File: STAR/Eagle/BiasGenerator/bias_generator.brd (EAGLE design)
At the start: 60.9 x 30.1 mm, 24 parts, among them J1 J30J-9J30, T1 750311838, U1 LT8300, U2 LT8330

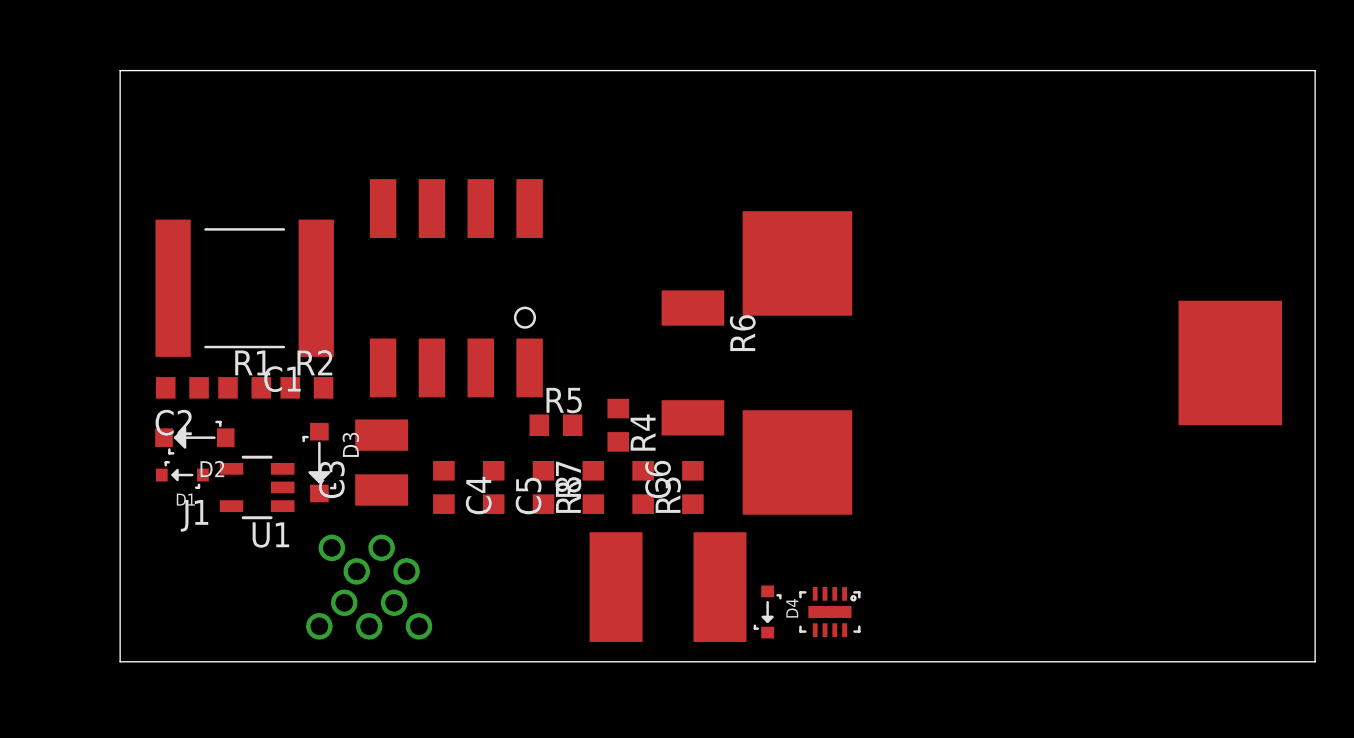
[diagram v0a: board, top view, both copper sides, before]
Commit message: datalogger differential pairs
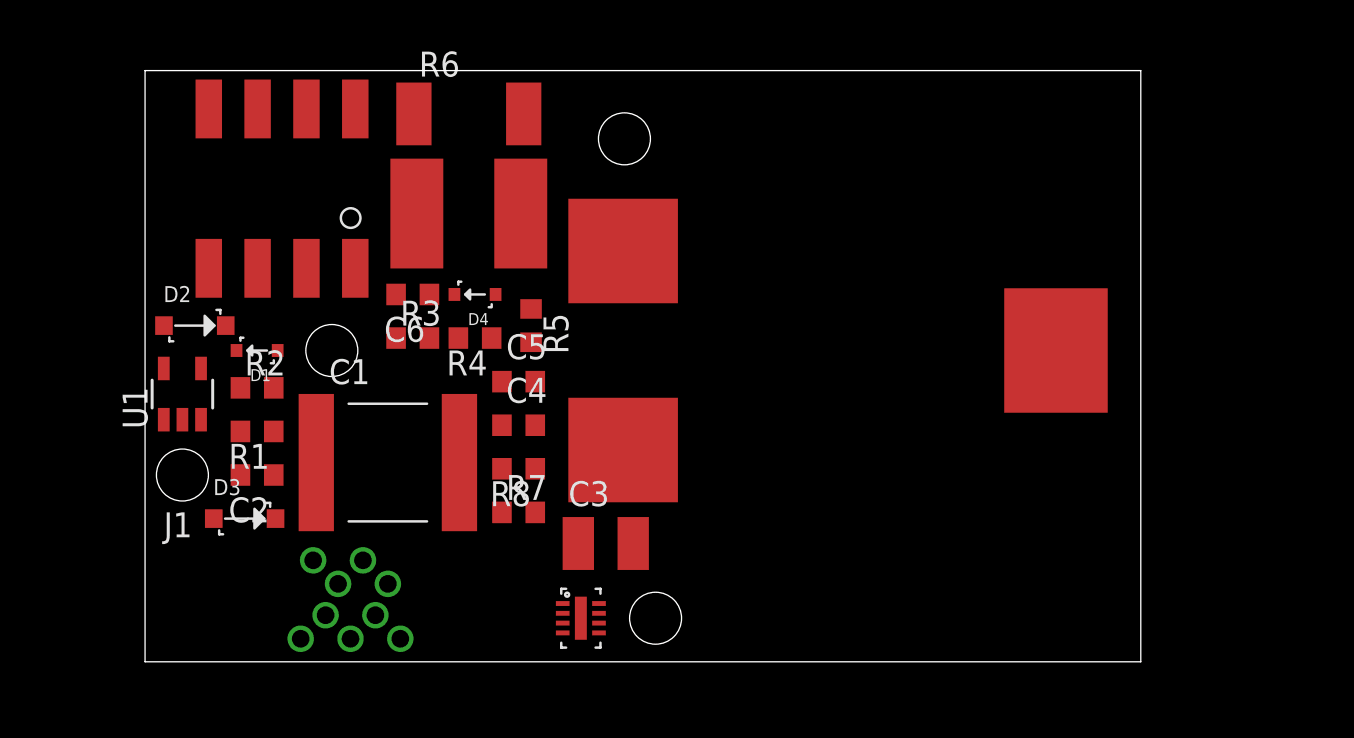
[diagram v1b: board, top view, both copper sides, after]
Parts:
- moved D4 22.0 mm to (16.8, 18.7), turned to 180 degrees
- moved C7 21.6 mm to (16.5, 22.9)
- moved C6 17.3 mm to (13.7, 18.7), turned to 180 degrees
- moved R6 17.1 mm to (16.5, 27.9), turned to 0 degrees
- moved R3 14.0 mm to (13.7, 16.5), turned to 0 degrees
- moved U2 12.7 mm to (22.2, 2.22), turned to 270 degrees
- moved C3 12.2 mm to (23.5, 6.03), turned to 0 degrees
- moved C1 11.5 mm to (12.4, 10.2), turned to 0 degrees
- moved T1 10.2 mm to (6.99, 24.1)
- moved L1 8.91 mm to (38.7, 15.9)
- moved R4 8.55 mm to (16.8, 16.5), turned to 180 degrees
- moved D1 7.41 mm to (5.71, 15.9)
- moved U1 6.10 mm to (1.91, 13.7), turned to 0 degrees
- moved C2 5.85 mm to (5.71, 9.53)
- moved D2 5.71 mm to (2.54, 17.1), turned to 0 degrees
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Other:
- board size 60.9 x 30.1 mm -> 50.8 x 30.1 mm

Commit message: M2 drills
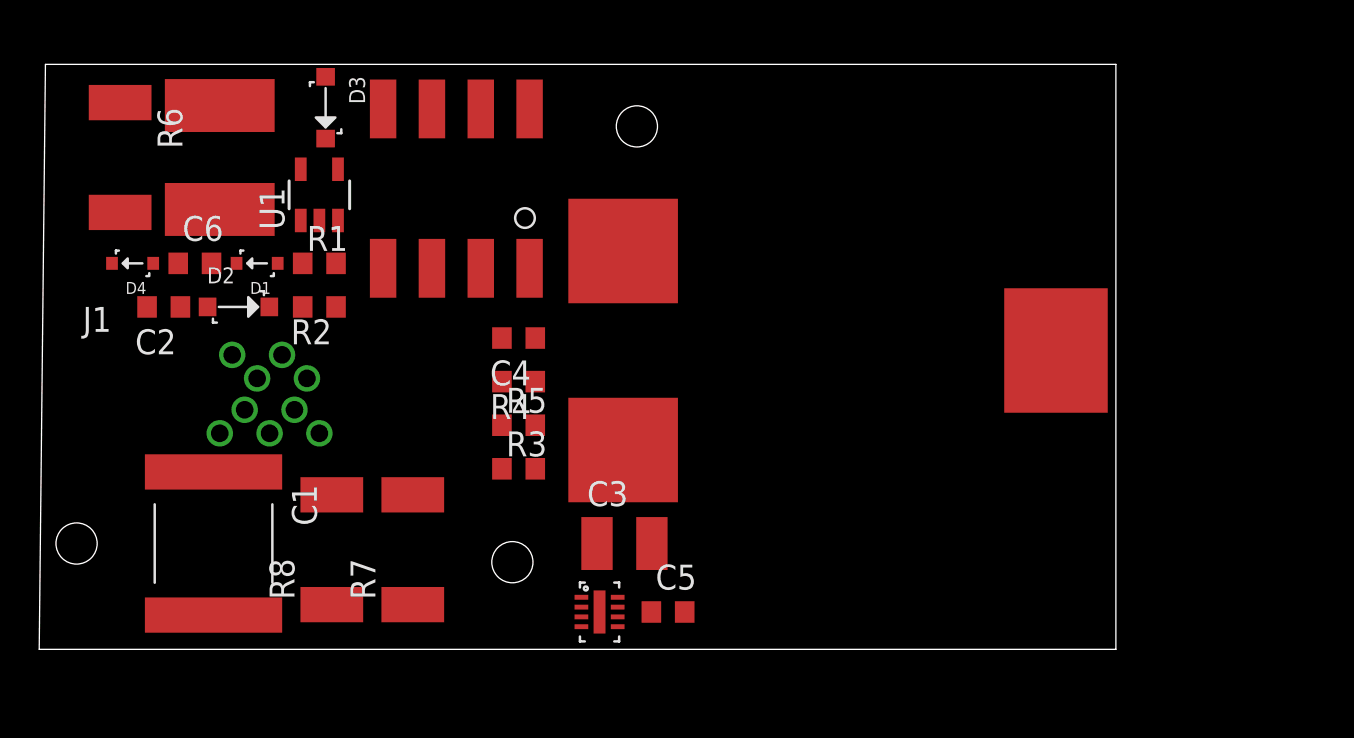
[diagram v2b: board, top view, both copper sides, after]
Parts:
- R7: value 47000 -> 47k; device resistor:R0603 -> resistor:R2512
- R8: value 3000 -> 3k; device resistor:R0603 -> resistor:R2512
- moved D3 21.4 mm to (9.21, 28.3), turned to 270 degrees
- moved R6 17.9 mm to (-1.27, 25.7), turned to 270 degrees
- moved D4 17.5 mm to (-0.64, 20.3)
- moved C5 14.0 mm to (26.7, 2.54)
- moved C7 13.0 mm to (3.81, 25.7), turned to 90 degrees
- moved U1 12.3 mm to (8.89, 23.8)
- moved J1 11.3 mm to (6.35, 13.7)
- moved C6 11.2 mm to (2.54, 20.3), turned to 0 degrees
- moved R8 10.4 mm to (9.53, 5.71), turned to 90 degrees
- moved C2 9.81 mm to (0.95, 18.1)
- moved C1 9.80 mm to (3.49, 6.03), turned to 270 degrees
- moved R1 9.14 mm to (8.89, 20.3), turned to 0 degrees
- moved T1 8.89 mm to (15.9, 24.1)
- moved R3 8.58 mm to (19.1, 9.84)
- moved R7 5.72 mm to (13.7, 5.71), turned to 90 degrees
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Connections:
- removed net N$18: J1.8
- removed net N$19: J1.9
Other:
- board size 50.8 x 30.1 mm -> 54.9 x 29.8 mm

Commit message: bias gen board
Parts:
- moved R7 5.08 mm to (18.7, 5.71)
- moved C1 5.08 mm to (8.57, 6.03)
- moved C2 5.08 mm to (6.03, 18.1)
- moved C6 5.08 mm to (7.62, 20.3)
- moved C7 5.08 mm to (8.89, 25.7)
- moved D1 5.08 mm to (10.8, 20.3)
- moved D4 5.08 mm to (4.45, 20.3)
- moved J1 5.08 mm to (11.4, 13.7)
- moved R1 5.08 mm to (14.0, 20.3)
- moved R2 5.08 mm to (14.0, 18.1)
- moved R6 5.08 mm to (3.81, 25.7)
- moved R8 5.08 mm to (14.6, 5.71)
- moved U1 5.08 mm to (14.0, 23.8)
- moved D2 5.08 mm to (9.84, 18.1)
- moved C3 5.08 mm to (29.5, 6.03)
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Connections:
- new net G: J1.3
- new net N$10: J1.9
- net +50V: now also J1.1, J1.2; no longer J1.3, J1.4
- net GND: now also J1.6; no longer J1.1, J1.2
- net VCC: now also J1.4; no longer J1.6
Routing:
- net +50V: track 0.00 -> 57.6 mm
- net GND: track 0.00 -> 55.8 mm, vias 0 -> 14
- net N$7: track 0.00 -> 48.8 mm, vias 0 -> 3
- net +20V: track 0.00 -> 43.6 mm
- net VCC: track 0.00 -> 43.1 mm
- net N$9: track 0.00 -> 36.7 mm, vias 0 -> 4
- net N$4: track 0.00 -> 17.4 mm, vias 0 -> 2
- net V_DIVIDE: track 0.00 -> 15.6 mm, vias 0 -> 2
- net N$5: track 0.00 -> 9.16 mm
- net N$6: track 0.00 -> 4.85 mm, vias 0 -> 2
- net N$2: track 0.00 -> 3.21 mm
- net N$1: track 0.00 -> 2.92 mm
- net N$3: track 0.00 -> 2.22 mm
- net N$11: track 0.00 -> 2.22 mm
- added copper zone on layer 1, net GND
- added copper zone on layer 16, net GND
- added copper zone on layer 1, net N$7
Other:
- board size 54.9 x 29.8 mm -> 54.6 x 29.8 mm

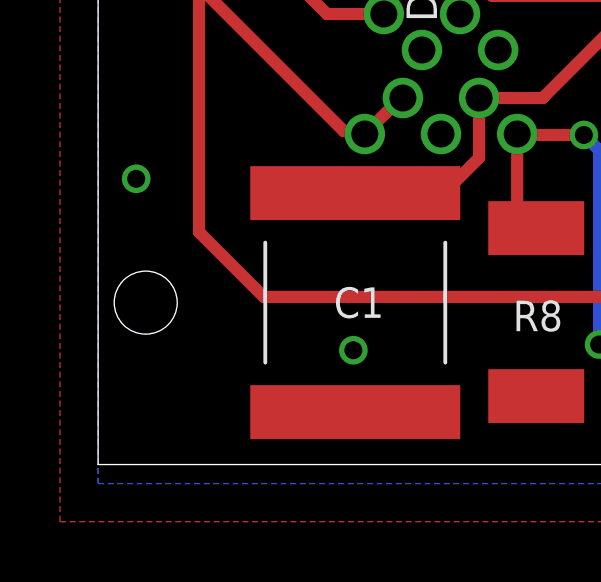
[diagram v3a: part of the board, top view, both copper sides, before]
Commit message: got rid of old STARduino routing
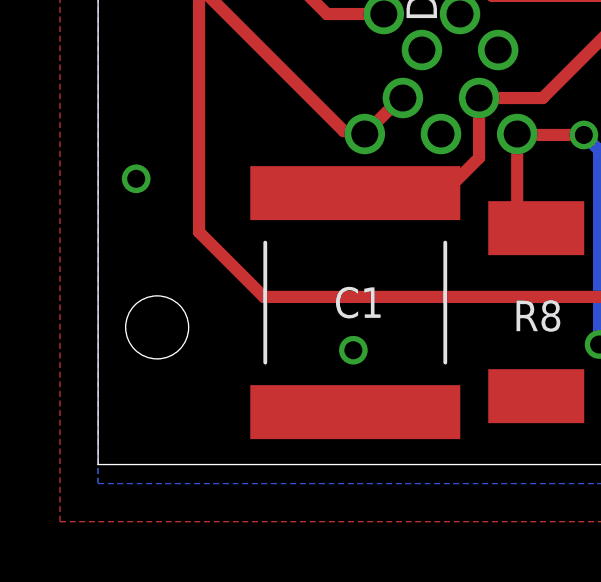
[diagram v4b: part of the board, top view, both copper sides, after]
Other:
- board text added: "Bias Generator"
- board text added: "Jan. 2017"
- board text added: "Rev. 1"
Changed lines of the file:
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@@
 <wire x1="0" y1="30.4675" x2="0" y2="0.635" width="0" layer="20"/>
 <hole x="30.1625" y="27.305" drill="2.1"/>
-<hole x="1.5875" y="6.0325" drill="2.1"/>
+<hole x="1.9685" y="5.207" drill="2.1"/>
 <hole x="23.8125" y="5.08" drill="2.1"/>
+<text x="49.4665" y="23.114" size="1.016" layer="22" font="vector" rot="MR0">Bias Generator</text>
+<text x="49.4665" y="20.066" size="1.016" layer="22" font="vector" rot="MR0">Jan. 2017</text>
+<text x="49.4665" y="21.3995" size="1.016" layer="22" font="vector" rot="MR0">Rev. 1</text>
 </plain>
 <attributes>

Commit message: screws
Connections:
- removed net G: J1.3
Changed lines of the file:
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@@
 <wire x1="0" y1="30.4675" x2="0" y2="0.635" width="0" layer="20"/>
 <hole x="30.1625" y="27.305" drill="2.1"/>
-<hole x="1.9685" y="5.207" drill="2.1"/>
+<hole x="2.413" y="5.207" drill="2.1"/>
 <hole x="23.8125" y="5.08" drill="2.1"/>
 <text x="49.4665" y="23.114" size="1.016" layer="22" font="vector" rot="MR0">Bias Generator</text>
 <text x="49.4665" y="20.066" size="1.016" layer="22" font="vector" rot="MR0">Jan. 2017</text>
 <text x="49.4665" y="21.3995" size="1.016" layer="22" font="vector" rot="MR0">Rev. 1</text>
+<circle x="2.413" y="5.207" radius="1.9" width="0.4064" layer="51"/>
+<circle x="23.8125" y="5.08" radius="1.9" width="0.4064" layer="51"/>
+<circle x="30.1625" y="27.305" radius="1.9" width="0.4064" layer="51"/>
 </plain>
 <attributes>
@@
 <contactref element="J1" pad="9"/>
 </signal>
-<signal name="G">
-<contactref element="J1" pad="3"/>
-</signal>
 </signals>
